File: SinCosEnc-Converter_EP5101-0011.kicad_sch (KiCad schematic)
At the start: 28 parts, among them U1 iC-NV, X1 Conn_02x06_Top_Bottom, X2 D-SUB-DR-15PCG-AB

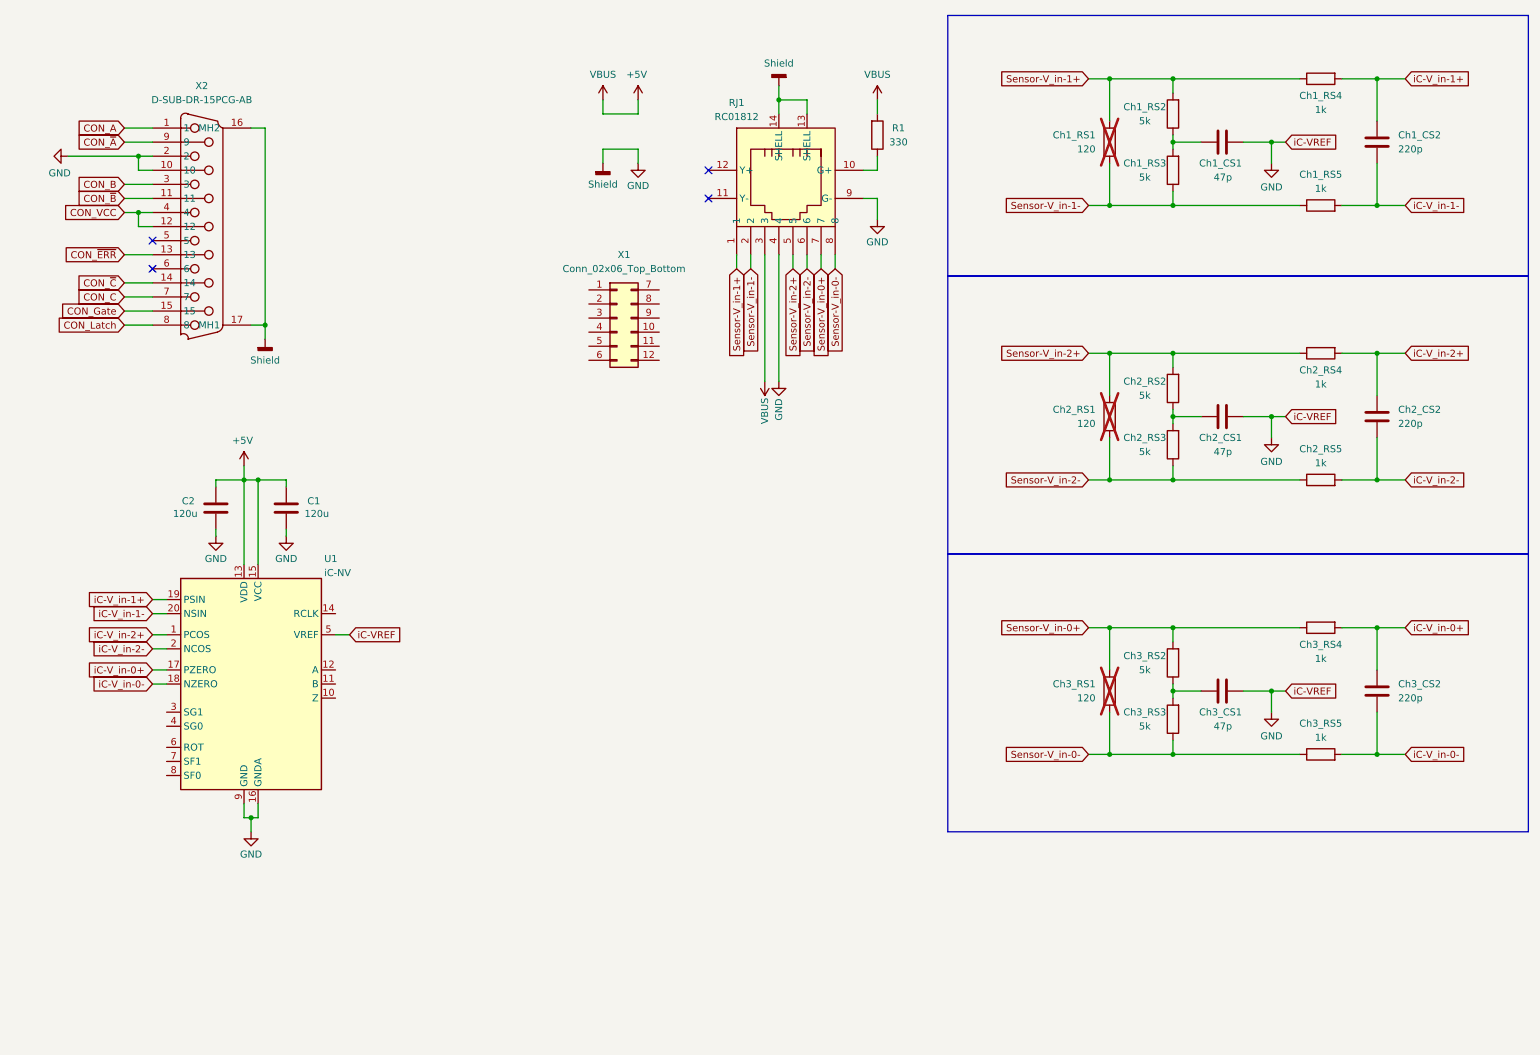
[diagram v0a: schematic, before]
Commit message: schematic finished ~90%, layout: just outline done added mounting concept pictures
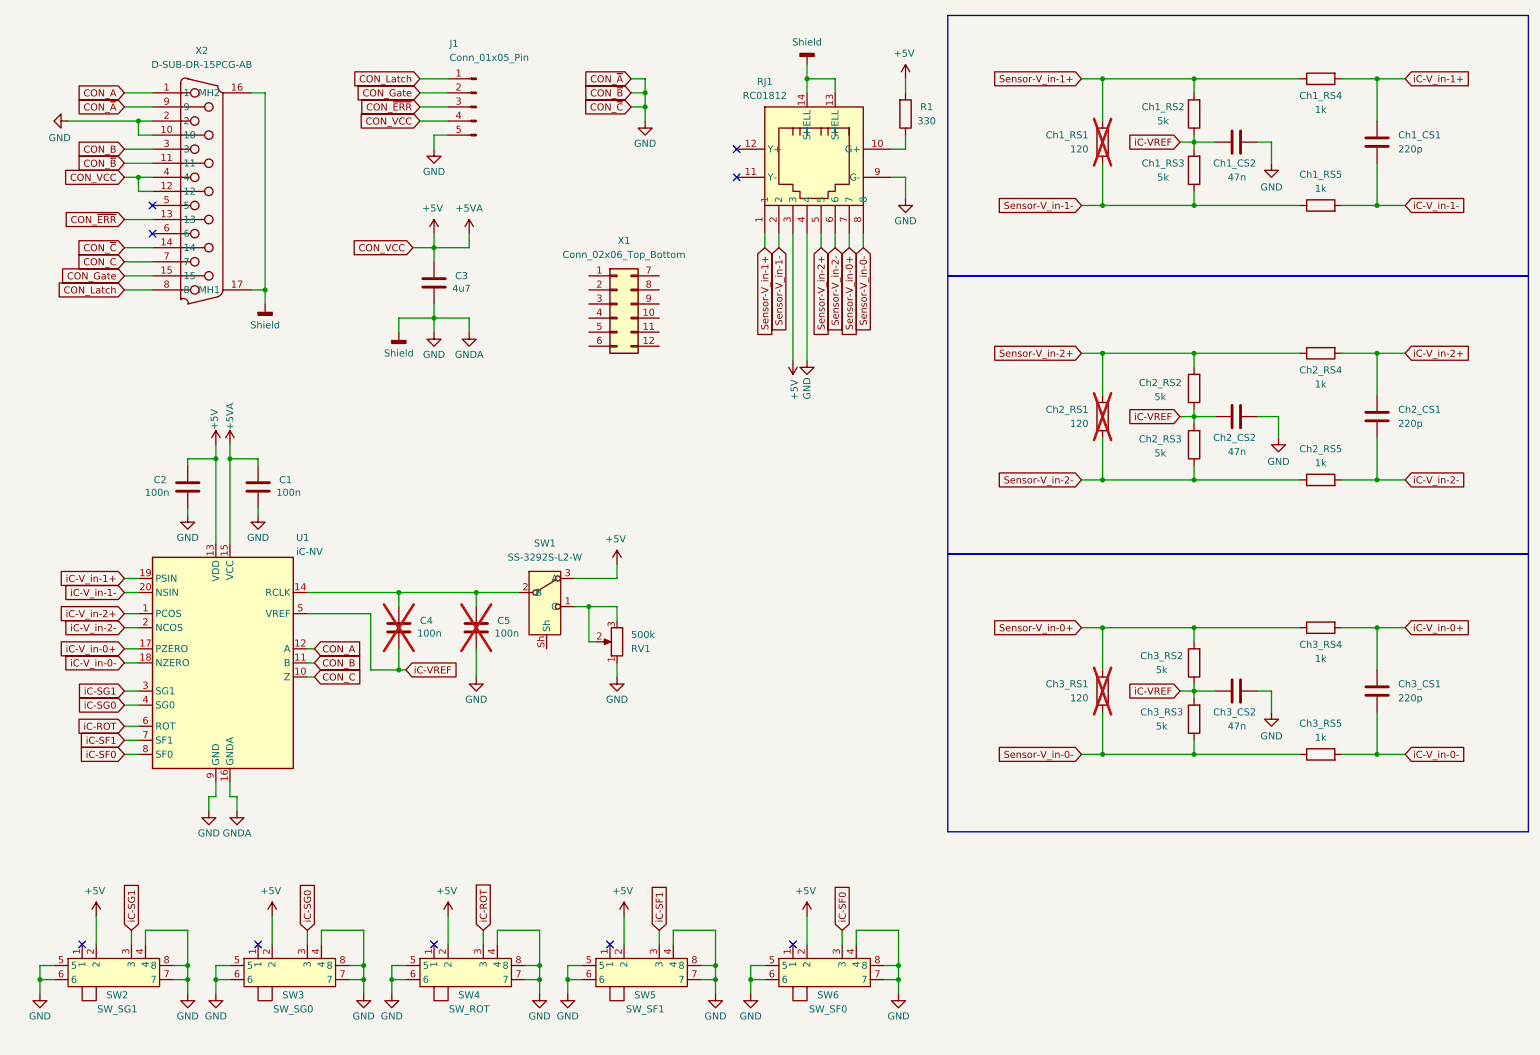
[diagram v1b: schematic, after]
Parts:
- added C3: 4u7, Capacitor_SMD:C_0603_1608Metric, symbol Device:C
- added C4, C5: 100n, Capacitor_SMD:C_0603_1608Metric, symbol Device:C
- added J1: Conn_01x05_Pin, Connector_JST:JST_XH_B5B-XH-A_1x05_P2.50mm_Vertical, symbol Connector:Conn_01x05_Pin
- added RV1: 500k, Potentiometer_THT:Potentiometer_Bourns_3296P_Horizontal, symbol Device:R_Potentiometer
- added SW1: SS-3292S-L2-W, CostumLibrary:SW-SMD_XKB_SS-3292S-L2-W, symbol CostumLibrary:SS-3292S-L2-W
- added SW2: SW_SG1, easyeda2kicad:SW-SMD_MSK13C02-BB, symbol easyeda2kicad:HXMSK13C02
- added SW3: SW_SG0, easyeda2kicad:SW-SMD_MSK13C02-BB, symbol easyeda2kicad:HXMSK13C02
- added SW4: SW_ROT, easyeda2kicad:SW-SMD_MSK13C02-BB, symbol easyeda2kicad:HXMSK13C02
- added SW5: SW_SF1, easyeda2kicad:SW-SMD_MSK13C02-BB, symbol easyeda2kicad:HXMSK13C02
- added SW6: SW_SF0, easyeda2kicad:SW-SMD_MSK13C02-BB, symbol easyeda2kicad:HXMSK13C02
- C1, C2: value 120u -> 100n
- Ch1_CS2: renamed from Ch1_CS1; value 47p -> 47n
- Ch2_CS2: renamed from Ch2_CS1; value 47p -> 47n
- Ch3_CS2: renamed from Ch3_CS1; value 47p -> 47n
- renumbered Ch1_CS2 to Ch1_CS1, Ch2_CS2 to Ch2_CS1, Ch3_CS2 to Ch3_CS1
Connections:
- net CON_VCC is gone; now on net +5V: X2.12, X2.4
- net CON_~{A} is gone; now on net GND: X2.9
- net CON_~{B} is gone; now on net GND: X2.11
- net CON_~{C} is gone; now on net GND: X2.14
- net +5V: now also C3.2, J1.4 (Pin_4), SW1.3 (A), SW2.2, SW3.2, SW4.2, SW5.2, SW6.2
- net CON_A: now also U1.12 (A)
- net CON_B: now also U1.11 (B)
- net CON_C: now also U1.10 (Z)
- net CON_Gate: now also J1.2 (Pin_2)
- net CON_Latch: now also J1.1 (Pin_1)
- net CON_~{ERR}: now also J1.3 (Pin_3)
- net GND: now also C3.1, C5.1, J1.5 (Pin_5), RV1.1, SW2.4, SW2.5, SW2.6, SW2.7, SW2.8, SW3.4, SW3.5, SW3.6, SW3.7, SW3.8, SW4.4, SW4.5, SW4.6, SW4.7, SW4.8, SW5.4, SW5.5, SW5.6, SW5.7, SW5.8, SW6.4, SW6.5, SW6.6, SW6.7, SW6.8; no longer U1.5 (VREF)
- net at U1.14 (RCLK): now also C4.2, C5.2, SW1.2 (B)
- net iC-SG1: now reaches U1.3 (SG1)
- net iC-SG1: now also SW2.3
- net iC-SG0: now reaches U1.4 (SG0)
- net iC-SG0: now also SW3.3
- net iC-ROT: now reaches U1.6 (ROT)
- net iC-ROT: now also SW4.3
- net iC-SF1: now reaches U1.7 (SF1)
- net iC-SF1: now also SW5.3
- net iC-SF0: now reaches U1.8 (SF0)
- net iC-SF0: now also SW6.3
- net iC-VREF: now reaches Ch2_CS2.1, Ch2_RS2.1, Ch2_RS3.2
- net iC-VREF: now also Ch1_CS2.1, Ch1_RS2.1, Ch1_RS3.2, Ch3_CS2.1, Ch3_RS2.1, Ch3_RS3.2, U1.5 (VREF), C4.1
- new net: RV1.2, RV1.3, SW1.1 (C)
- no-connect marks 4 -> 9
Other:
- moved on the sheet: C1, C2, Ch1_CS2, Ch1_RS1, Ch1_RS2, Ch1_RS3, Ch2_CS2, Ch2_RS1, Ch2_RS2, Ch2_RS3, Ch3_CS2, Ch3_RS1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

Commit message: minor progress
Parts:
- removed X1: Conn_02x06_Top_Bottom, Connector_PinHeader_2.54mm:PinHeader_2x06_P2.54mm_Horizontal, symbol Connector_Generic:Conn_02x06_Top_Bottom
- added J2: Conn_02x05_Top_Bottom, Connector_PinHeader_2.54mm:PinHeader_2x05_P2.54mm_Horizontal, symbol Connector_Generic:Conn_02x05_Odd_Even
- SW1: value SS-3292S-L2-W -> SW_RCLK
- renumbered Ch1_RS2 to Ch1_RS1, Ch1_RS3 to Ch1_RS2, Ch1_RS4 to Ch1_RS3, Ch1_RS5 to Ch1_RS4, Ch1_RS1 to Ch1_RS5, Ch2_RS2 to Ch2_RS1, Ch2_RS3 to Ch2_RS2, Ch2_RS4 to Ch2_RS3, Ch2_RS5 to Ch2_RS4, Ch2_RS1 to Ch2_RS5, Ch3_RS2 to Ch3_RS1, Ch3_RS3 to Ch3_RS2, Ch3_RS4 to Ch3_RS3, Ch3_RS5 to Ch3_RS4, Ch3_RS1 to Ch3_RS5
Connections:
- net +5V: now also J2.3 (Pin_3)
- net GND: now also J2.10 (Pin_10), J2.4 (Pin_4), J2.9 (Pin_9)
- net Sensor-V_in-0+: now also J2.7 (Pin_7)
- net Sensor-V_in-0-: now also J2.8 (Pin_8)
- net Sensor-V_in-1+: now also J2.1 (Pin_1)
- net Sensor-V_in-1-: now also J2.2 (Pin_2)
- net Sensor-V_in-2+: now also J2.5 (Pin_5)
- net Sensor-V_in-2-: now also J2.6 (Pin_6)
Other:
- note added: "Configs: -> 1V_{pp} ChX_RS5 (120 ohm) populated 3x SW_SG0: SW_SG1: SW_ROT: SW_SF0: SW_SF1: SW_RCLK: RV1: set to X ohm => Gain: 8 -> 11µA_{pp} ChX_RS5 all removed/not placed SW_SG0: open | high SW_SG1: low | low SW_ROT: SW_SF0: SW_SF1: SW_RCLK: high | poti RV1: / | 500k => Gain: 4 | 7.1"
- note added: "Converter config bits"
- note added: "Converter iC"
- note added: "DSUB/DB15 plug (to EP5101-0011)"
- note added: "Frontend 1 - channel A - SIN"
- note added: "Frontend 2 - channel B - COS"
- note added: "Frontend 3 - channel C - ZERO"
- note added: "NOTE Pin 9&10 shield"
- note added: "NOTE Positions: NotConnected (1) | High (2) | Low (4)"
- note added: "PinHeader Input"
- note added: "RJ45 Input"
- note added: "central big cap"
- note added: "other pins"
- moved on the sheet: C1, C2, C3, C4, C5, J1, R1, RJ1, RV1, SW1, U1, X2

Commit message: finished schematics for v0.9.0, PCB ToDo
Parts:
- removed C1, C2, C4, C5: 100n, Capacitor_SMD:C_0603_1608Metric, symbol Device:C
- removed Ch1_CS1, Ch2_CS1, Ch3_CS1: 220p, Capacitor_SMD:C_0603_1608Metric, symbol Device:C
- removed Ch1_CS2, Ch2_CS2, Ch3_CS2: 47n, Capacitor_SMD:C_0603_1608Metric, symbol Device:C
- removed Ch1_RS1, Ch1_RS2, Ch2_RS1, Ch2_RS2, Ch3_RS1, Ch3_RS2: 5k, Resistor_SMD:R_0603_1608Metric, symbol Device:R
- removed Ch1_RS3, Ch1_RS4, Ch2_RS3, Ch2_RS4, Ch3_RS3, Ch3_RS4: 1k, Resistor_SMD:R_0603_1608Metric, symbol Device:R
- removed Ch1_RS5, Ch2_RS5, Ch3_RS5: 120, Resistor_SMD:R_0603_1608Metric, symbol Device:R
- removed J2: Conn_02x05_Top_Bottom, Connector_PinHeader_2.54mm:PinHeader_2x05_P2.54mm_Horizontal, symbol Connector_Generic:Conn_02x05_Odd_Even
- removed R1: 330, Resistor_SMD:R_0603_1608Metric, symbol Device:R
- removed RJ1: RC01812, easyeda2kicad:RJ45-TH_RC01812, symbol easyeda2kicad:RC01812
- removed RV1: 500k, Potentiometer_THT:Potentiometer_Bourns_3296P_Horizontal, symbol Device:R_Potentiometer
- removed SW1: SW_RCLK, CostumLibrary:SW-SMD_XKB_SS-3292S-L2-W, symbol CostumLibrary:SS-3292S-L2-W
- removed SW2: SW_SG1, easyeda2kicad:SW-SMD_MSK13C02-BB, symbol easyeda2kicad:HXMSK13C02
- removed SW3: SW_SG0, easyeda2kicad:SW-SMD_MSK13C02-BB, symbol easyeda2kicad:HXMSK13C02
- removed SW4: SW_ROT, easyeda2kicad:SW-SMD_MSK13C02-BB, symbol easyeda2kicad:HXMSK13C02
- removed SW5: SW_SF1, easyeda2kicad:SW-SMD_MSK13C02-BB, symbol easyeda2kicad:HXMSK13C02
- removed SW6: SW_SF0, easyeda2kicad:SW-SMD_MSK13C02-BB, symbol easyeda2kicad:HXMSK13C02
- removed U1: iC-NV, Package_SO:TSSOP-20_4.4x6.5mm_P0.65mm, symbol CostumLibrary:iC-NV
- added C6: 100n, Capacitor_SMD:C_0603_1608Metric, symbol Device:C
- added JP1: SingleEnded_A, Jumper:SolderJumper-2_P1.3mm_Open_RoundedPad1.0x1.5mm, symbol Jumper:SolderJumper_2_Open
- added JP2: CON_~{A} to GND, Jumper:SolderJumper-2_P1.3mm_Open_RoundedPad1.0x1.5mm, symbol Jumper:SolderJumper_2_Open
- added JP3: SingleEnded_B, Jumper:SolderJumper-2_P1.3mm_Open_RoundedPad1.0x1.5mm, symbol Jumper:SolderJumper_2_Open
- added JP4: CON_~{B} to GND, Jumper:SolderJumper-2_P1.3mm_Open_RoundedPad1.0x1.5mm, symbol Jumper:SolderJumper_2_Open
- added JP5: SingleEnded_C, Jumper:SolderJumper-2_P1.3mm_Open_RoundedPad1.0x1.5mm, symbol Jumper:SolderJumper_2_Open
- added JP6: CON_~{C} to GND, Jumper:SolderJumper-2_P1.3mm_Open_RoundedPad1.0x1.5mm, symbol Jumper:SolderJumper_2_Open
- added U2: AM26LS31CDR, easyeda2kicad:SOIC-16_L9.9-W3.9-P1.27-LS6.0-BL, symbol easyeda2kicad:AM26LS31CDR
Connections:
- net +5V: now also C6.2, U2.16 (VCC)
- net GND: now also C6.1, JP2.2 (B), JP4.2 (B), JP6.2 (B), U2.12 (!G), U2.4 (G), U2.8 (GND); no longer X2.11, X2.14, X2.9
- net CON_A renamed CON_A+
- net CON_A+: now also JP1.2 (B), U2.2 (1Y)
- net CON_B renamed CON_B+
- net CON_B+: now also JP3.2 (B), U2.6 (2Y)
- net CON_C renamed CON_C-
- net CON_C-: now also JP6.1 (A), U2.11 (3Z)
- new net CON_A-: JP2.1 (A), U2.3 (1Z), X2.9
- new net CON_B-: JP4.1 (A), U2.5 (2Z), X2.11
- new net CON_C+: JP5.2 (B), U2.10 (3Y), X2.14
- new net TTL_Sig_A: JP1.1 (A), U2.1 (1A)
- new net TTL_Sig_B: JP3.1 (A), U2.7 (2A)
- new net TTL_Sig_C: JP5.1 (A), U2.9 (3A)
- no-connect marks 9 -> 5
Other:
- added sheet iC-NV (interpolator.kicad_sch)
- note added: "Differential Driver"
- note added: "main interpolator/conversion IC"
- note removed: "Configs: -> 1V_{pp} ChX_RS5 (120 ohm) populated 3x SW_SG0: SW_SG1: SW_ROT: SW_SF0: SW_SF1: SW_RCLK: RV1: set to X ohm => Gain: 8 -> 11µA_{pp} ChX_RS5 all removed/not placed SW_SG0: open | high SW_SG1: low | low SW_ROT: SW_SF0: SW_SF1: SW_RCLK: high | poti RV1: / | 500k => Gain: 4 | 7.1"
- note removed: "Converter config bits"
- note removed: "Converter iC"
- note removed: "Frontend 1 - channel A - SIN"
- note removed: "Frontend 2 - channel B - COS"
- note removed: "Frontend 3 - channel C - ZERO"
- note removed: "NOTE Pin 9&10 shield"
- note removed: "NOTE Positions: NotConnected (1) | High (2) | Low (4)"
- note removed: "PinHeader Input"
- note removed: "RJ45 Input"
- title: (none) -> Header and Outputs
- moved on the sheet: C3, J1, X2
